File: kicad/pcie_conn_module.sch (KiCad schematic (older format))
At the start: 1 part, among them P1 pcie_1x_edge

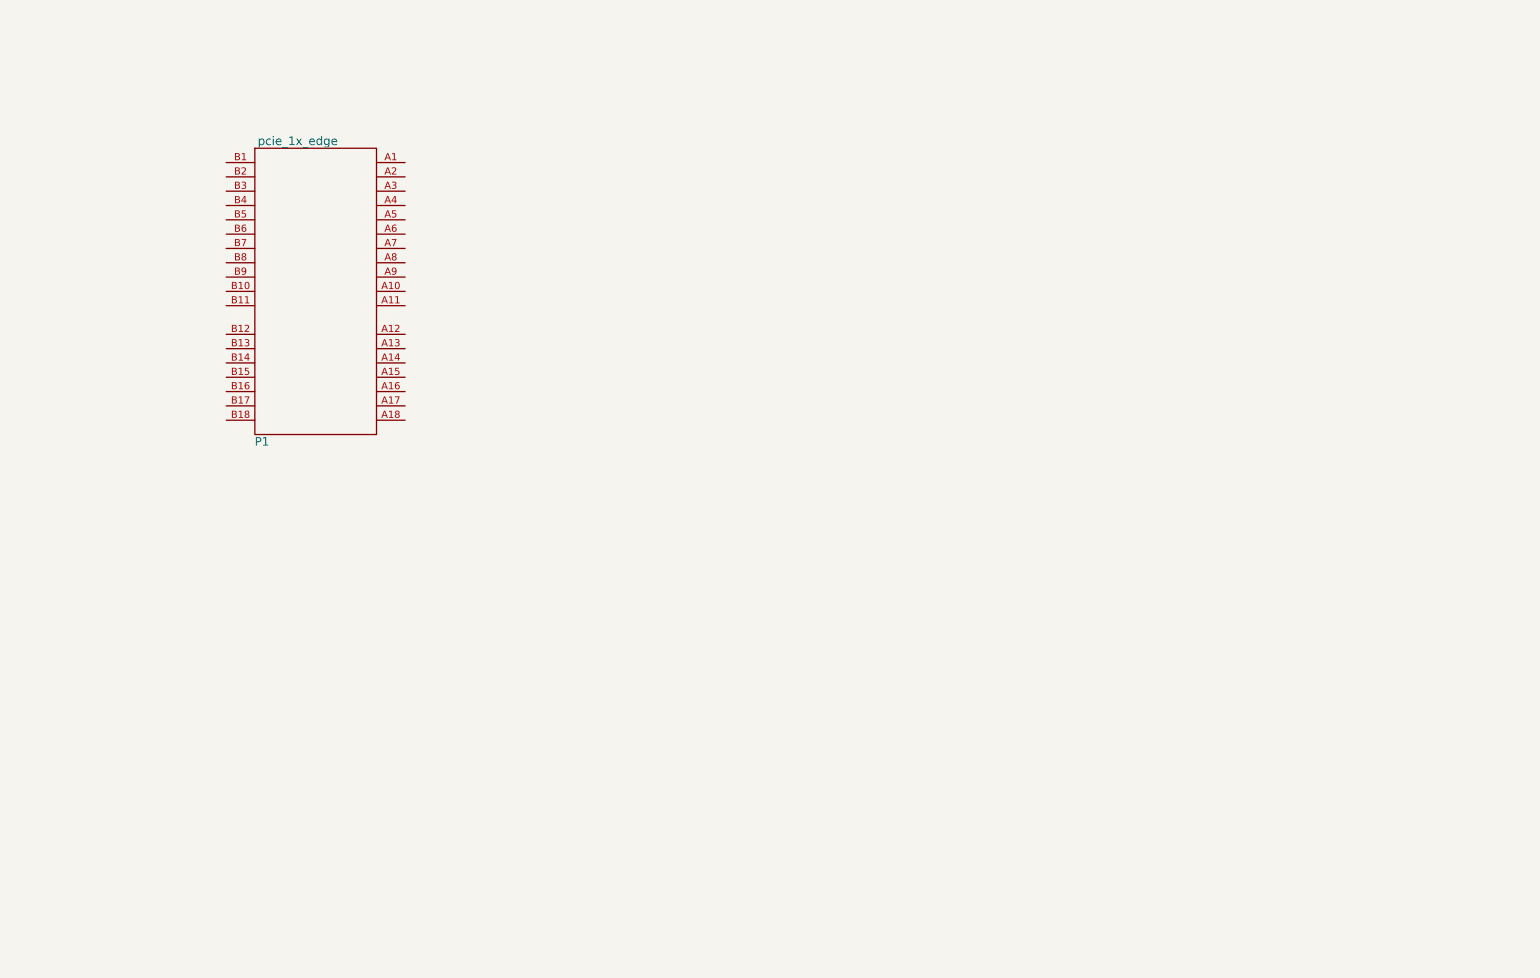
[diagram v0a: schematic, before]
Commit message: add mux & eeprom
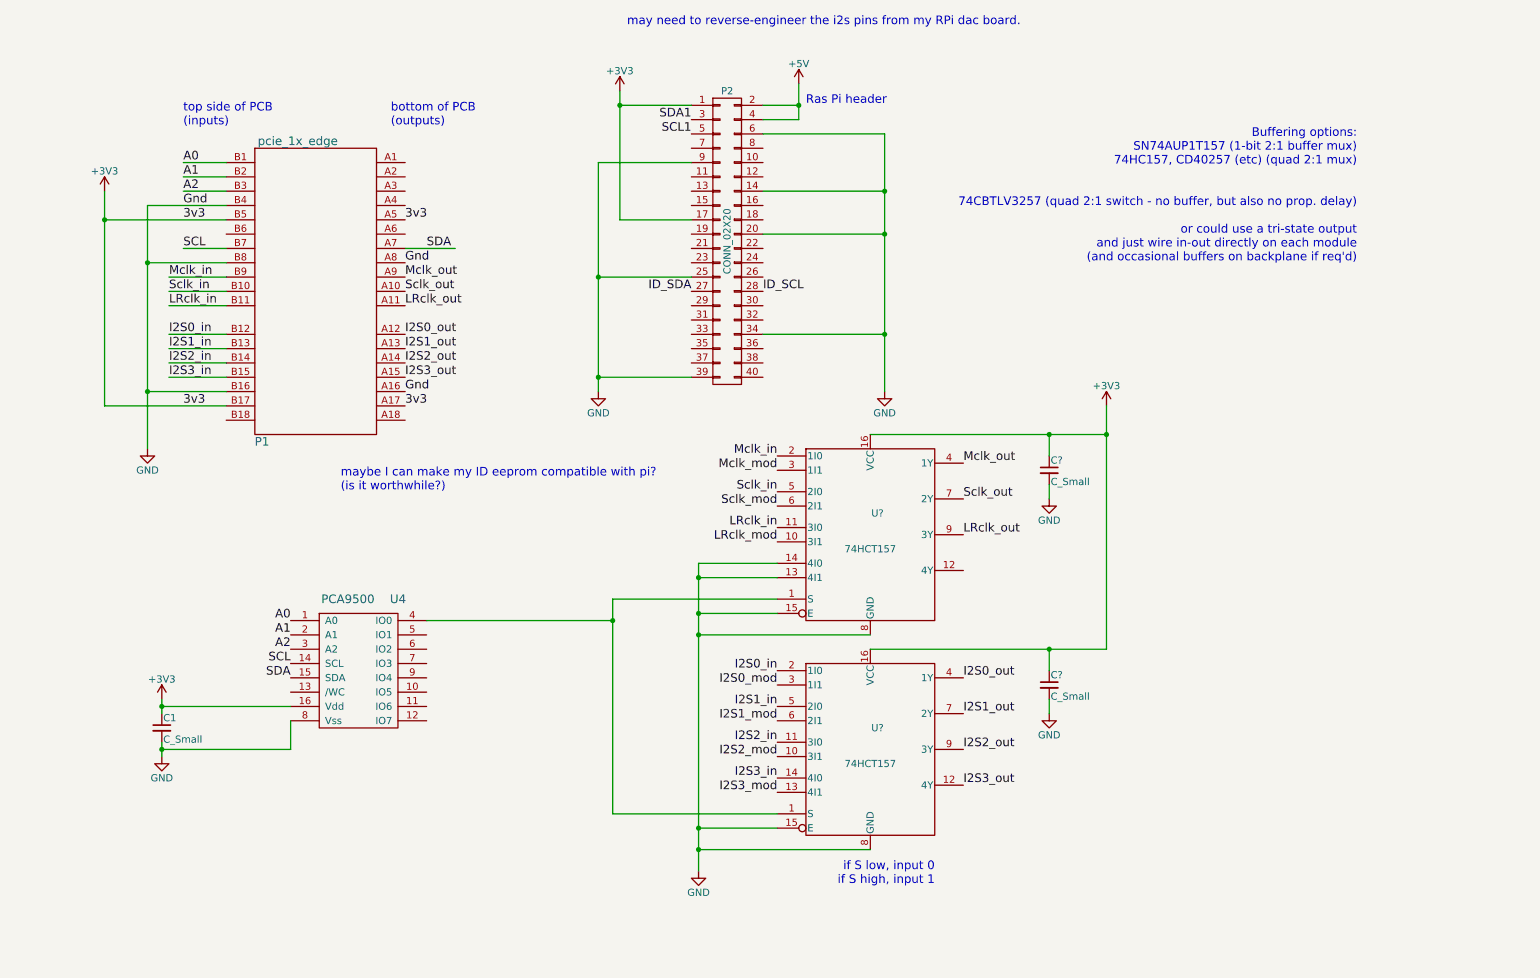
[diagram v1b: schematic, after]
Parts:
- added C1, C? (x2): C_Small, Capacitors_SMD:C_0805_HandSoldering, symbol C_Small
- added P2: CONN_02X20, Pin_Headers:Pin_Header_Straight_2x20, symbol CONN_02X20
- added U4: PCA9500, symbol PCA9500
- added U? (x2): 74HCT157, symbol 74HCT157
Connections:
- net Sclk_out: now reaches P1.A10
- net Sclk_out: now also U?.7 (2Y)
- net LRclk_out: now reaches P1.A11
- net LRclk_out: now also U?.9 (3Y)
- net I2S0_out: now reaches P1.A12
- net I2S0_out: now also U?.4 (1Y)
- net I2S1_out: now reaches P1.A13
- net I2S1_out: now also U?.7 (2Y)
- net I2S2_out: now reaches P1.A14
- net I2S2_out: now also U?.9 (3Y)
- net I2S3_out: now reaches P1.A15
- net I2S3_out: now also U?.12 (4Y)
- net GND: now reaches P1.A16
- net GND: now also P1.A8, P1.B16, P1.B4, P1.B8, C1.2, C?.2, C?.2, P2.14 (P14), P2.20 (P20), P2.25 (P25), P2.34 (P34), P2.39 (P39), P2.6 (P6), P2.9 (P9), U4.8 (Vss), U?.13 (4I1), U?.14 (4I0), U?.15 (E), U?.15 (E), U?.8 (GND), U?.8 (GND)
- net +3V3: now reaches P1.A17
- net +3V3: now also P1.A5, P1.B17, P1.B5, C1.1, C?.1, C?.1, P2.1 (P1), P2.17 (P17), U4.16 (Vdd), U?.16 (VCC), U?.16 (VCC)
- net SDA: now reaches P1.A7
- net SDA: now also U4.15 (SDA)
- net Mclk_out: now reaches P1.A9
- net Mclk_out: now also U?.4 (1Y)
- net A0: now reaches P1.B1
- net A0: now also U4.1 (A0)
- net Sclk_in: now reaches P1.B10
- net Sclk_in: now also U?.5 (2I0)
- net LRclk_in: now reaches P1.B11
- net LRclk_in: now also U?.11 (3I0)
- net I2S0_in: now reaches P1.B12
- net I2S0_in: now also U?.2 (1I0)
- net I2S1_in: now reaches P1.B13
- net I2S1_in: now also U?.5 (2I0)
- net I2S2_in: now reaches P1.B14
- net I2S2_in: now also U?.11 (3I0)
- net I2S3_in: now reaches P1.B15
- net I2S3_in: now also U?.14 (4I0)
- net A1: now reaches P1.B2
- net A1: now also U4.2 (A1)
- net A2: now reaches P1.B3
- net A2: now also U4.3 (A2)
- net SCL: now reaches P1.B7
- net SCL: now also U4.14 (SCL)
- net Mclk_in: now reaches P1.B9
- net Mclk_in: now also U?.2 (1I0)
- new net: U4.4 (IO0), U?.1 (S), U?.1 (S)
- new net +5V: P2.2 (P2), P2.4 (P4)
- new net I2S0_mod: U?.3 (1I1)
- new net I2S1_mod: U?.6 (2I1)
- new net I2S2_mod: U?.10 (3I1)
- new net I2S3_mod: U?.13 (4I1)
- new net ID_SCL: P2.28 (P28)
- new net ID_SDA: P2.27 (P27)
- new net LRclk_mod: U?.10 (3I1)
- new net Mclk_mod: U?.3 (1I1)
- new net SCL1: P2.5 (P5)
- new net SDA1: P2.3 (P3)
- new net Sclk_mod: U?.6 (2I1)
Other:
- note added: "Buffering options:\nSN74AUP1T157 (1-bit 2:1 buffer mux)\n74HC157, CD40257 (etc) (quad 2:1 mux)\n\n\n74CBTLV3257 (quad 2:1 switch - no buffer, but also no prop. delay)\n\nor could use a tri-state output \nand just wire in-out directly on each module \n(and occasional buffers on backplane if req'd)\n"
- note added: "Ras Pi header"
- note added: "bottom of PCB\n(outputs)"
- note added: "if S low, input 0\nif S high, input 1"
- note added: "may need to reverse-engineer the i2s pins from my RPi dac board.\n"
- note added: "maybe I can make my ID eeprom compatible with pi?\n(is it worthwhile?)"
- note added: "top side of PCB\n(inputs)"

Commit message: first draft schematic
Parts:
- removed P2: CONN_02X20, Pin_Headers:Pin_Header_Straight_2x20, symbol CONN_02X20
- added P2, P5: CONN_01X18, Pin_Headers:Pin_Header_Straight_1x18, symbol CONN_01X18
- added P3, P6: CONN_01X03, Pin_Headers:Pin_Header_Straight_1x03, symbol CONN_01X03
- added P4: CONN_01X08, Pin_Headers:Pin_Header_Straight_1x08, symbol CONN_01X08
- added R1: 10k, Resistors_SMD:R_0805_HandSoldering, symbol R
- U1, U2: renamed from U?; footprint (none) -> Housings_SOIC:SOIC-16_3.9x9.9mm_Pitch1.27mm
- U4: footprint (none) -> Housings_SSOP:TSSOP-16_4.4x5mm_Pitch0.65mm
- gave numbers to parts that had none: 2
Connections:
- net labels removed: +5V, ID_SCL, ID_SDA, SCL1, SDA1
- wire segments 78 -> 120
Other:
- note added: "pi sound pins taken from BCM2835 peripheral datasheet"
- note added: "should add test points for each pin on PCIe header (and maybe pi header too) for first prototype!"
- note removed: "Ras Pi header"
- note removed: "may need to reverse-engineer the i2s pins from my RPi dac board.\n"
